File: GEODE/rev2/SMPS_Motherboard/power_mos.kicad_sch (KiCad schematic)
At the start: 8 parts, among them Q1201 SQJQ186E-T1_GE3, Q1202 SQJQ186E-T1_GE3, Q1203 SQJQ186E-T1_GE3, Q1204 SQJQ186E-T1_GE3

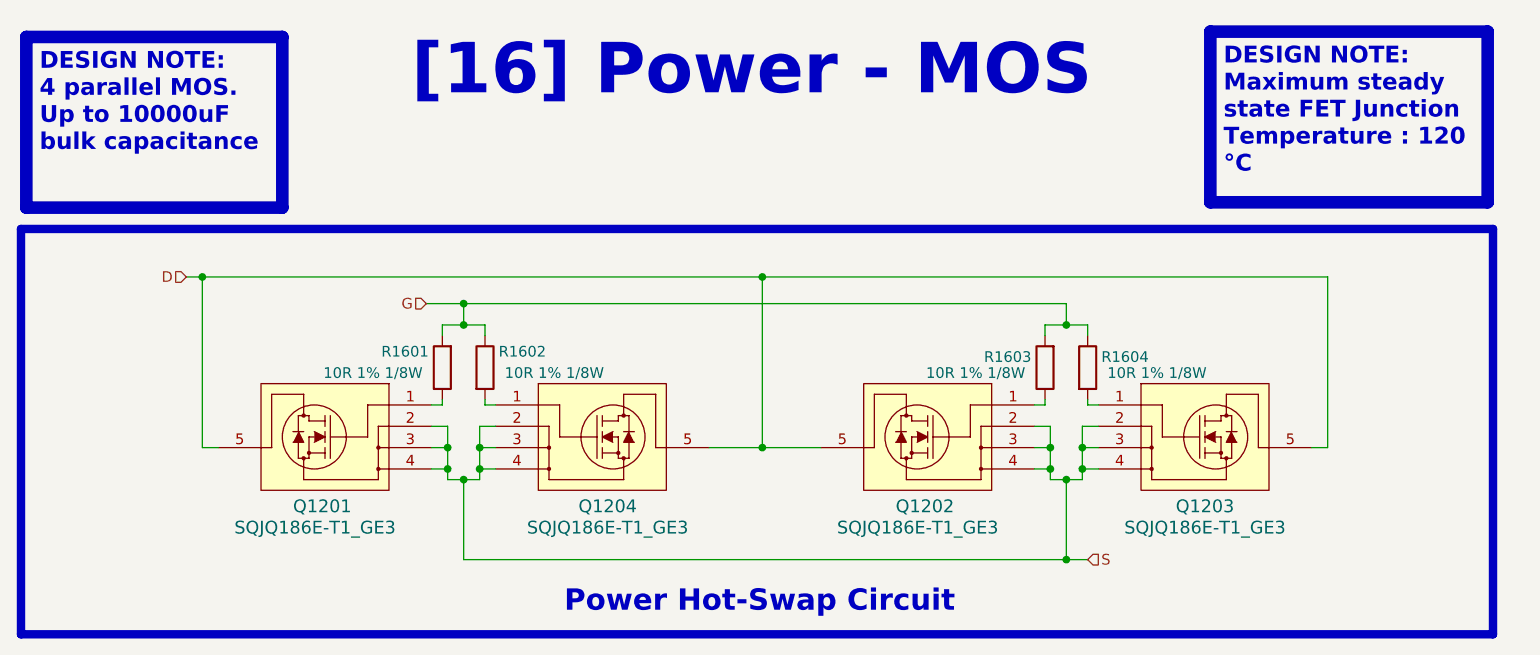
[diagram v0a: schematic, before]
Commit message: changed connectors, removed can, added fuse, disconnected EXTVCC in power generation
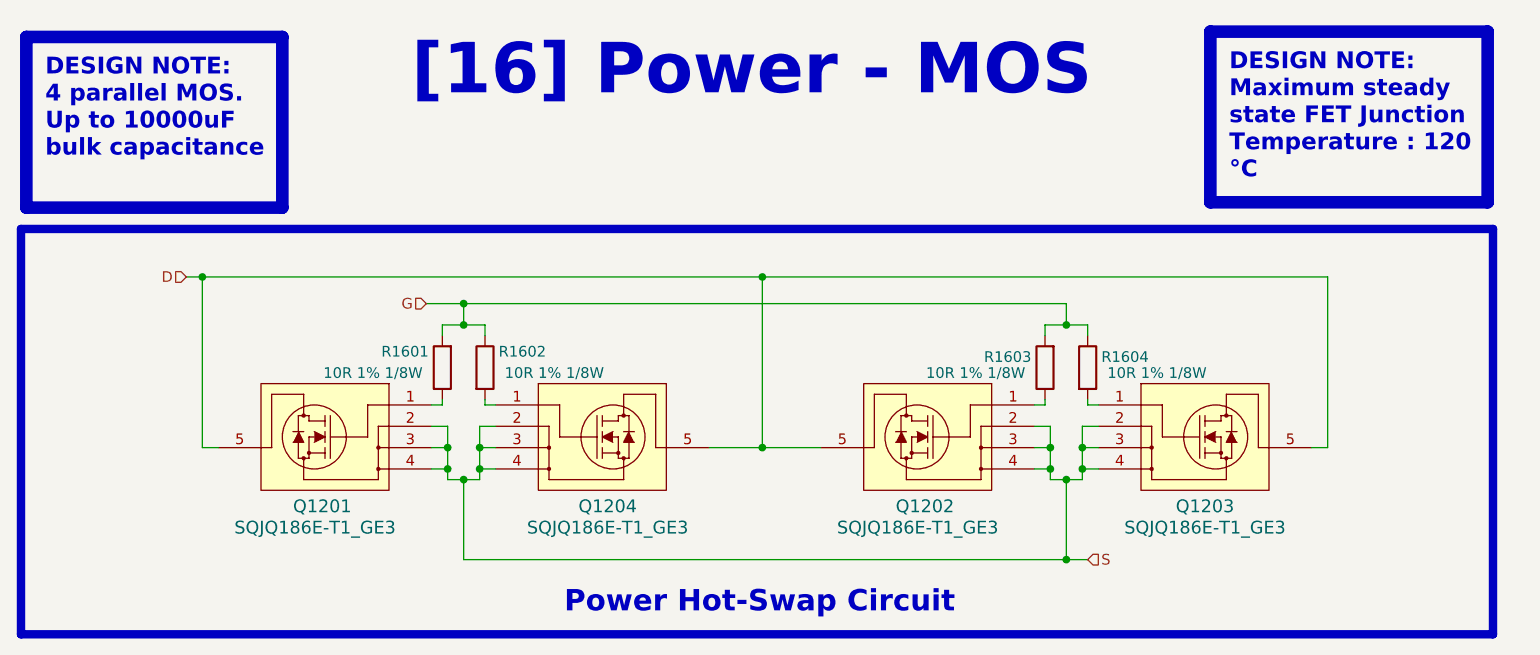
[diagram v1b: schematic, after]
